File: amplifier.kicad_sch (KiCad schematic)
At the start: 15 parts, among them T1 T1-1T-KK81, U5 LM4040AIM3, U8 OPA357AIDBVR

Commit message: 3d models update
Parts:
- D3: MP (none) -> 933976380215
- R22, R23: MP ERJ3EKF49R9V -> ERJ3EKF25R5V
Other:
- title: SiPM Board -> Amplifier
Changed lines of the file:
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@@
 	(paper "A4")
 	(title_block
-		(title "SiPM Board")
-		(date "2025-09-06")
-		(rev "0.2.1")
+		(title "Amplifier")
+		(date "2025-09-07")
+		(rev "0.2.3")
 		(company "Vadym Vikulin")
 		(comment 7 "Temperature Correction (~21 mV/K)")
@@
 				(size 1.27 1.27)
 			)
-			(justify right top)
+			(justify left top)
 		)
 	)
@@
 			)
 		)
-		(property "MP" "ERJ3EKF49R9V"
+		(property "MP" "ERJ3EKF25R5V"
 			(at 193.04 74.93 0)
 			(effects
@@
 			)
 		)
+		(property "MP" "933976380215"
+			(at 86.36 74.93 90)
+			(effects
+				(font
+					(size 1.27 1.27)
+				)
+				(hide yes)
+			)
+		)
 		(pin "3"
 		)
@@
 			)
 		)
-		(property "MP" "ERJ3EKF49R9V"
+		(property "MP" "ERJ3EKF25R5V"
 			(at 193.04 101.6 0)
 			(effects

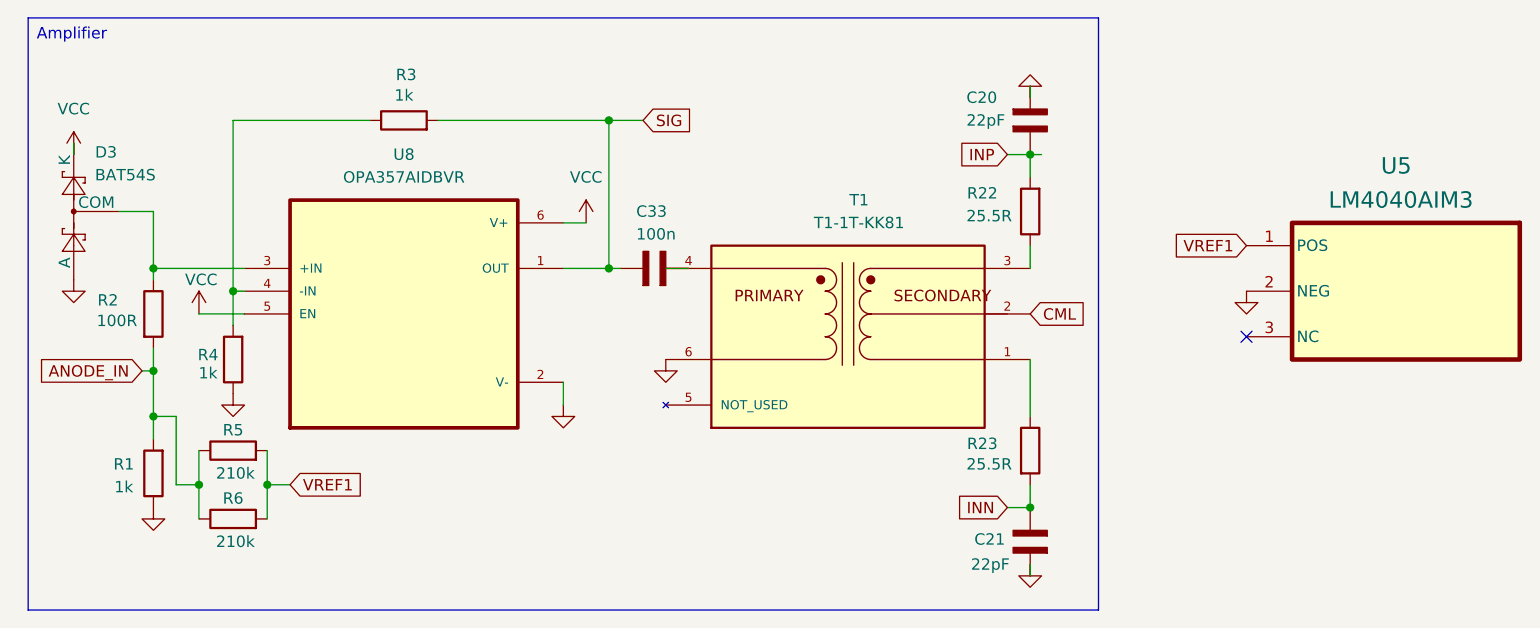
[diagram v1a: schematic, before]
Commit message: Modular SiPM board
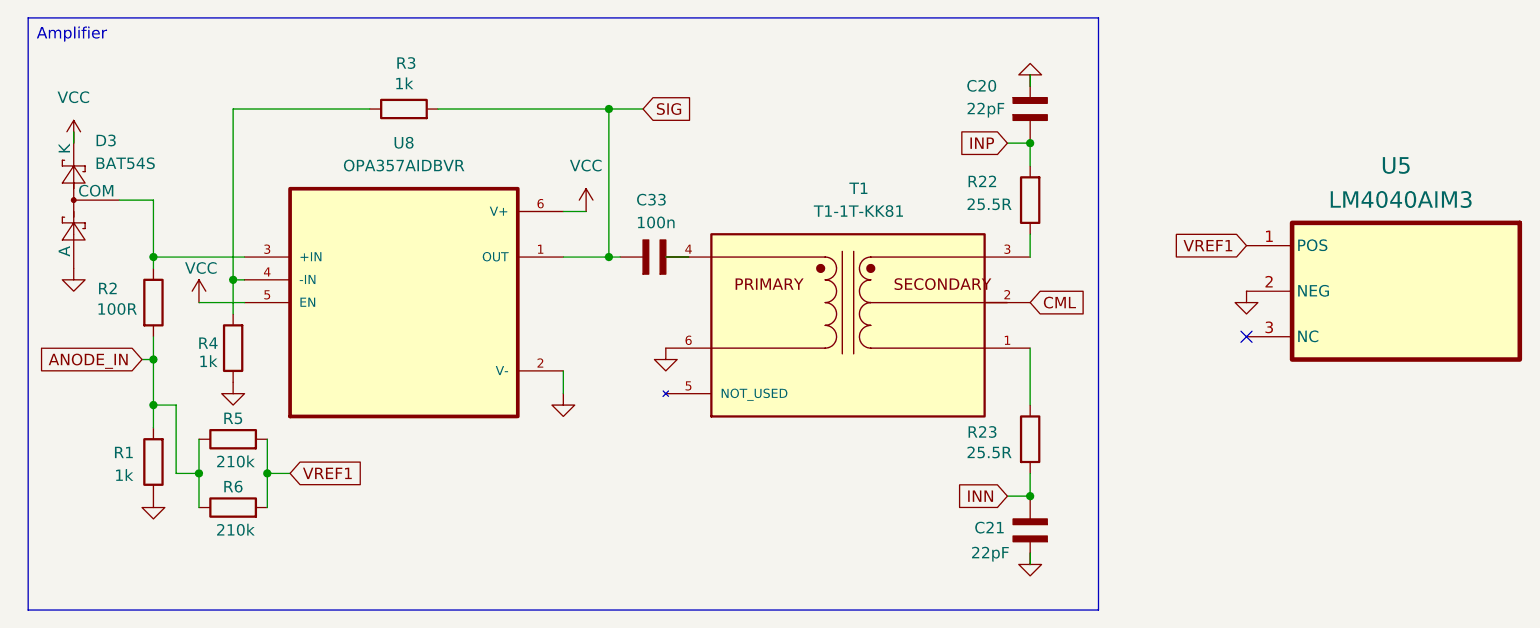
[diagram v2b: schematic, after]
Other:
- moved on the sheet: C20, C21, C33, D3, R1, R2, R22, R23, R3, R4, R5, R6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
